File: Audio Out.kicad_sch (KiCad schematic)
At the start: 14 parts

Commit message: Fixed ultralibrarian library with capital letter difference
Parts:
- U9: footprint UltraLibrarian:D8_TEX -> Ultralibrarian:D8_TEX
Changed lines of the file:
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@@
       (effects (font (size 1.27 1.27)))
     )
-    (property "Footprint" "UltraLibrarian:D8_TEX" (at 131.445 52.705 0)
+    (property "Footprint" "Ultralibrarian:D8_TEX" (at 131.445 52.705 0)
       (effects (font (size 1.27 1.27)) hide)
     )
@@
       (effects (font (size 1.27 1.27)))
     )
-    (property "Footprint" "UltraLibrarian:D8_TEX" (at 131.445 106.045 0)
+    (property "Footprint" "Ultralibrarian:D8_TEX" (at 131.445 106.045 0)
       (effects (font (size 1.27 1.27)) hide)
     )
@@
       (effects (font (size 1.27 1.27)))
     )
-    (property "Footprint" "UltraLibrarian:D8_TEX" (at 156.21 144.78 0)
+    (property "Footprint" "Ultralibrarian:D8_TEX" (at 156.21 144.78 0)
       (effects (font (size 1.27 1.27)) hide)
     )

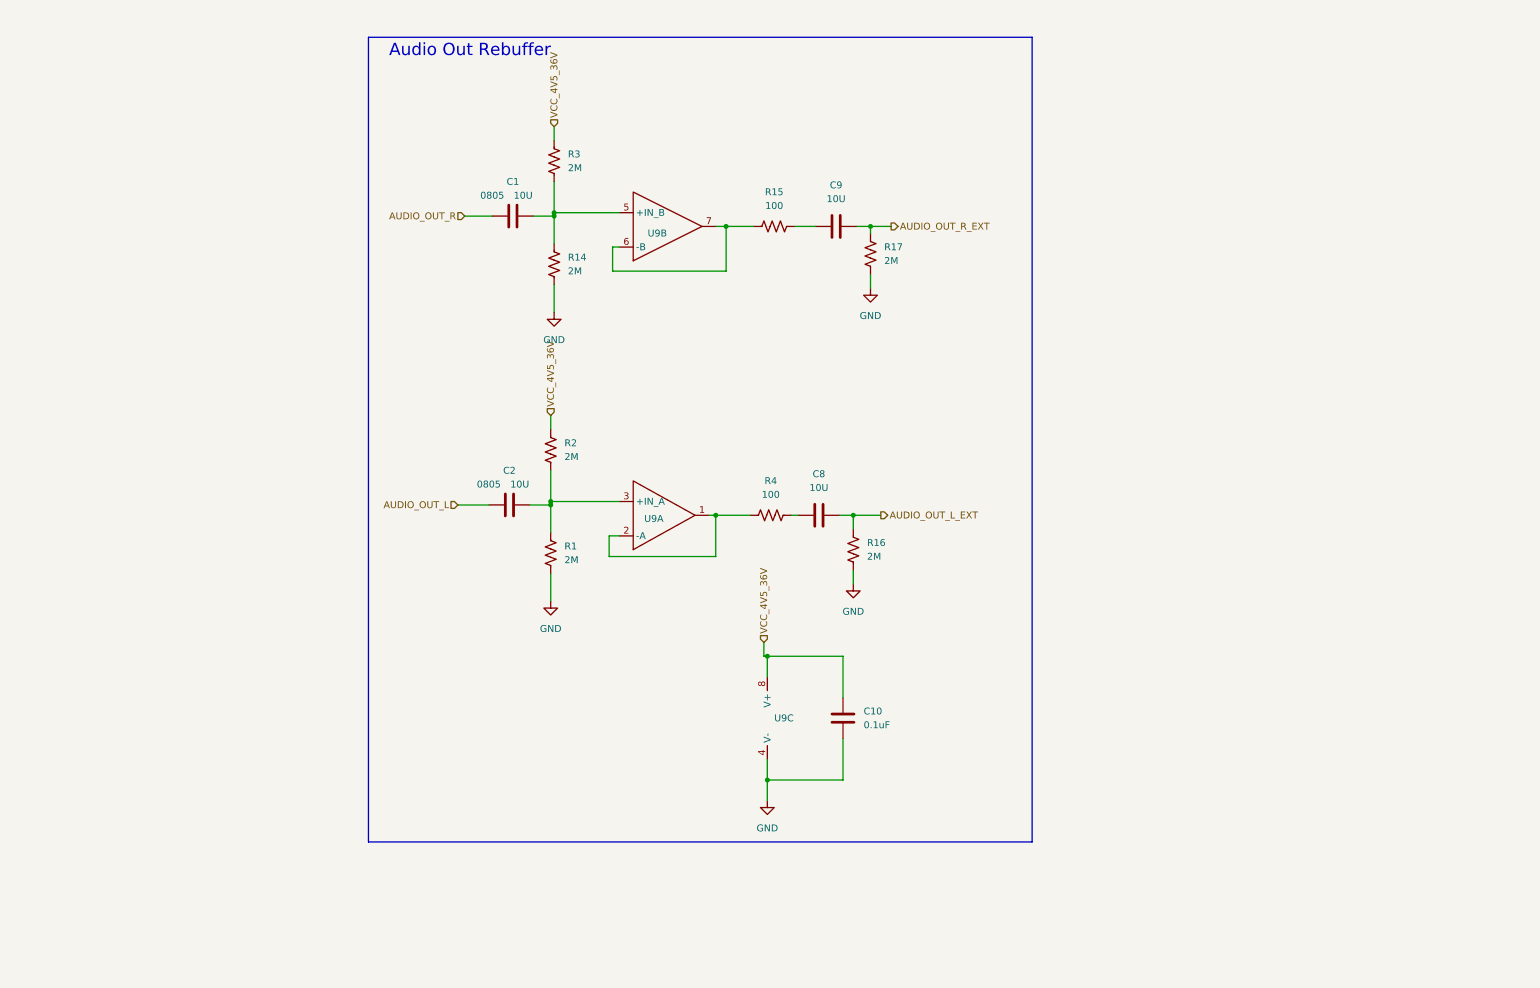
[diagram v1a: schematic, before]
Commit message: added knob headers, MIDI in header
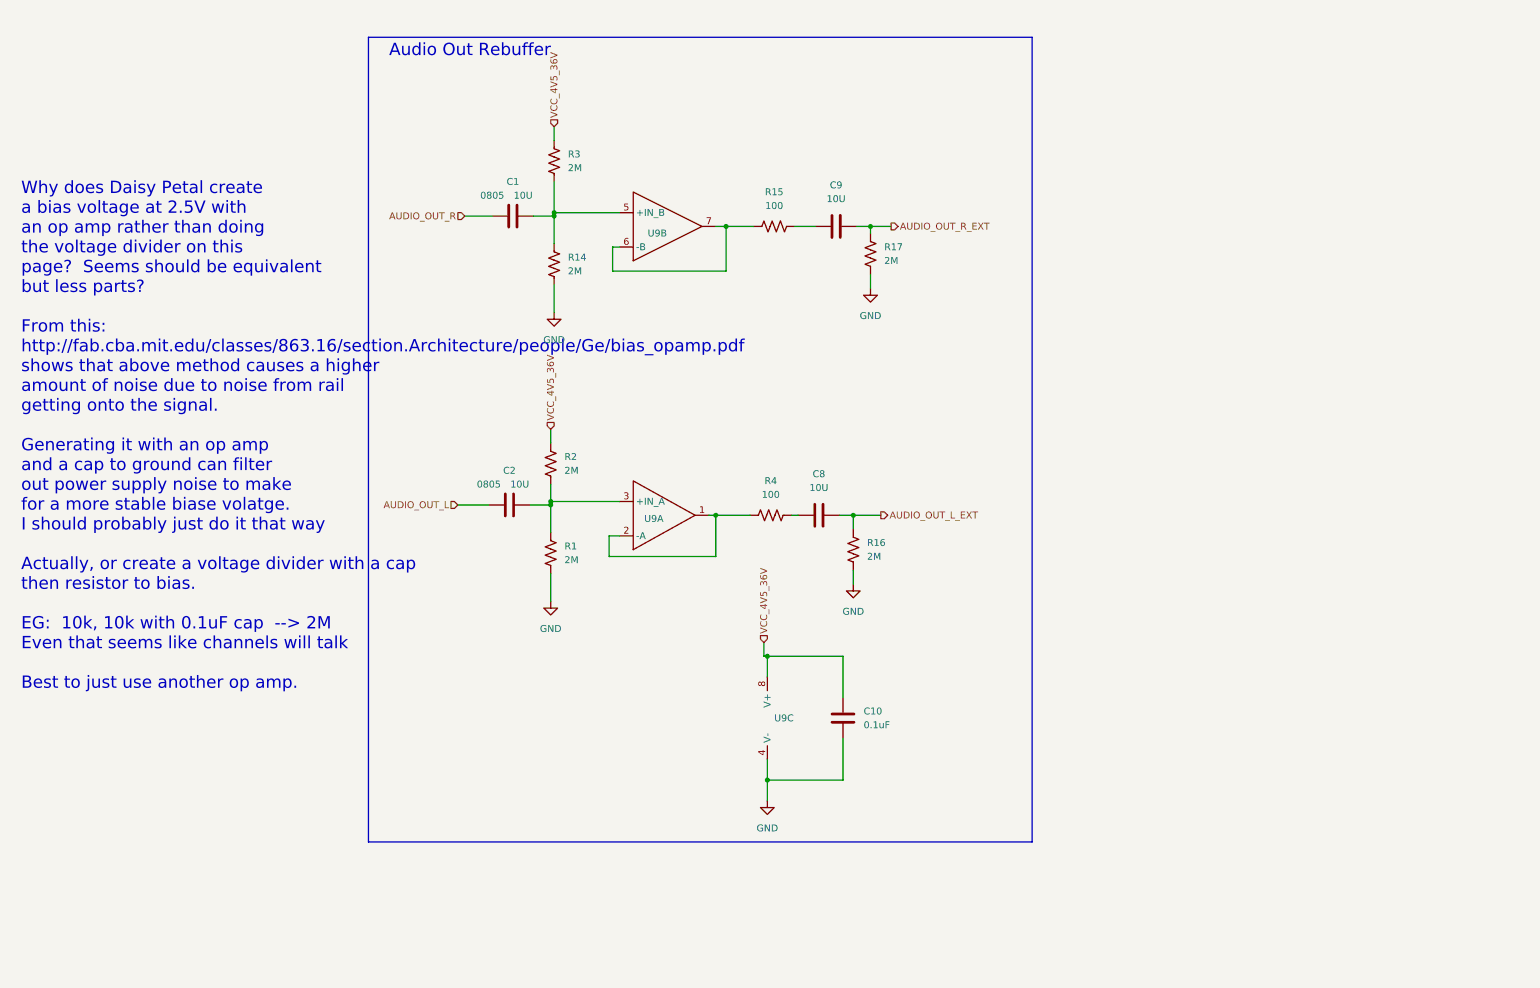
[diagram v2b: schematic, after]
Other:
- note added: "Why does Daisy Petal create a bias voltage at 2.5V with an op amp rather than doing the voltage divider on this page? Seems should be equivalent but less parts? From this: http://fab.cba.mit.edu/classes/863.16/section.Architecture/people/Ge/bias_opamp.pdf shows that above method causes a higher amount of noise due to noise from rail getting onto the signal. Generating it with an op amp and a cap 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"
- moved on the sheet: R2
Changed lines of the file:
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@@
     (stroke (width 0) (type default))
   )
-  (wire (pts (xy 113.665 97.79) (xy 113.665 103.505))
+  (wire (pts (xy 113.665 100.33) (xy 113.665 103.505))
     (stroke (width 0) (type default))
   )
@@
     (stroke (width 0) (type default))
   )
-  (wire (pts (xy 113.665 87.63) (xy 113.665 90.17))
+  (wire (pts (xy 113.665 90.17) (xy 113.665 92.71))
     (stroke (width 0) (type default))
   )
@@
     (effects (font (size 2.27 2.27)) (justify left bottom))
   )
+  (text "Why does Daisy Petal create\na bias voltage at 2.5V with\nan op amp rather than doing\nthe voltage divider on this\npage?  Seems should be equivalent\nbut less parts?\n\nFrom this:\nhttp://fab.cba.mit.edu/classes/863.16/section.Architecture/people/Ge/bias_opamp.pdf\nshows that above method causes a higher\namount of noise due to noise from rail\ngetting onto the signal.\n\nGenerating it with an op amp\nand a cap to ground can filter\nout power supply noise to make\nfor a more stable biase volatge.\nI should probably just do it that way\n\nActually, or create a voltage divider with a cap\nthen resistor to bias.\n\nEG:  10k, 10k with 0.1uF cap  --> 2M\nEven that seems like channels will talk\n\nBest to just use another op amp."
+    (at 15.875 138.43 0)
+    (effects (font (size 2.27 2.27)) (justify left bottom))
+  )
   (hierarchical_label "AUDIO_OUT_L" (shape input) (at 96.52 104.14 180) (fields_autoplaced)
     (effects (font (size 1.27 1.27)) (justify right))
   )
-  (hierarchical_label "VCC_4V5_36V" (shape input) (at 113.665 87.63 90) (fields_autoplaced)
+  (hierarchical_label "VCC_4V5_36V" (shape input) (at 113.665 90.17 90) (fields_autoplaced)
     (effects (font (size 1.27 1.27)) (justify left))
   )
@@
     )
   )
-  (symbol (lib_id "Device:R_US") (at 113.665 93.98 0) (unit 1)
-    (in_bom yes) (on_board yes) (dnp no) (fields_autoplaced)
-    (property "Reference" "R2" (at 116.205 92.71 0)
-      (effects (font (size 1.27 1.27)) (justify left))
-    )
-    (property "Value" "2M" (at 116.205 95.25 0)
-      (effects (font (size 1.27 1.27)) (justify left))
-    )
-    (property "Footprint" "Resistor_SMD:R_0402_1005Metric" (at 114.681 94.234 90)
-      (effects (font (size 1.27 1.27)) hide)
-    )
-    (property "Datasheet" "~" (at 113.665 93.98 0)
-      (effects (font (size 1.27 1.27)) hide)
-    )
+  (symbol (lib_id "Device:R_US") (at 113.665 96.52 0) (unit 1)
+    (in_bom yes) (on_board yes) (dnp no) (fields_autoplaced)
+    (property "Reference" "R2" (at 116.205 95.25 0)
+      (effects (font (size 1.27 1.27)) (justify left))
+    )
+    (property "Value" "2M" (at 116.205 97.79 0)
+      (effects (font (size 1.27 1.27)) (justify left))
+    )
+    (property "Footprint" "Resistor_SMD:R_0402_1005Metric" (at 114.681 96.774 90)
+      (effects (font (size 1.27 1.27)) hide)
+    )
+    (property "Datasheet" "~" (at 113.665 96.52 0)
+      (effects (font (size 1.27 1.27)) hide)
+    )

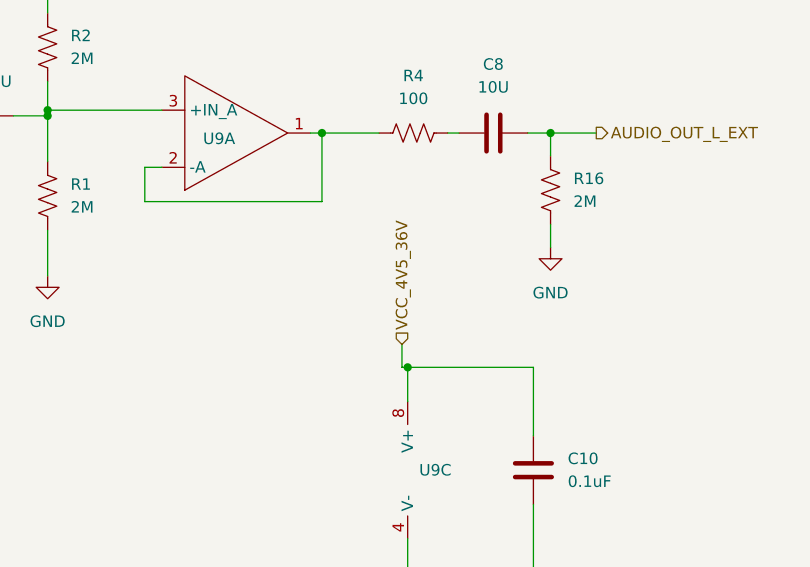
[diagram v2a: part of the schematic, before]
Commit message: Placeholder for speaker driver
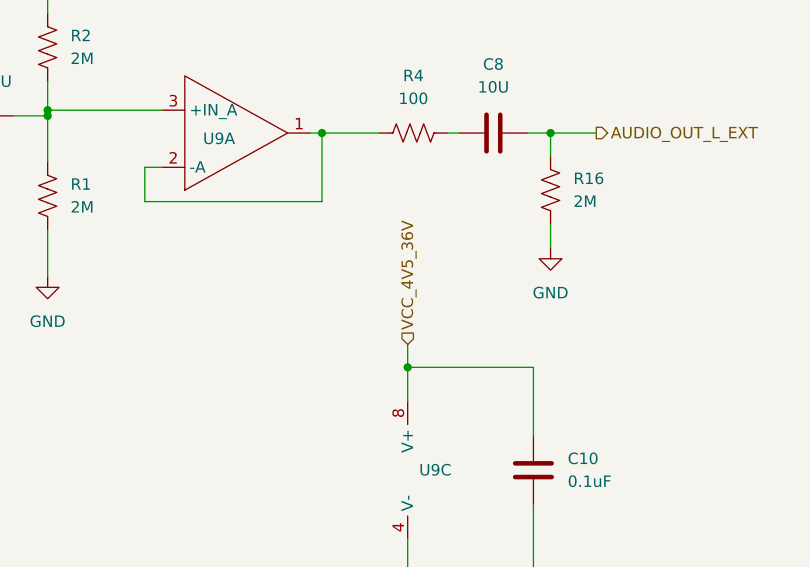
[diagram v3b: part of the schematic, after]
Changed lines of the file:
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@@
-    (stroke (width 0) (type default))
-  )
-  (wire (pts (xy 153.035 132.08) (xy 153.67 132.08))
     (stroke (width 0) (type default))
   )
@@
     (stroke (width 0) (type default))
   )
-  (wire (pts (xy 153.035 129.54) (xy 153.035 132.08))
+  (wire (pts (xy 153.67 129.54) (xy 153.67 132.08))
     (stroke (width 0) (type default))
   )
@@
     (effects (font (size 1.27 1.27)) (justify left))
   )
-  (hierarchical_label "VCC_4V5_36V" (shape input) (at 153.035 129.54 90) (fields_autoplaced)
+  (hierarchical_label "VCC_4V5_36V" (shape input) (at 153.67 129.54 90) (fields_autoplaced)
     (effects (font (size 1.27 1.27)) (justify left))
   )

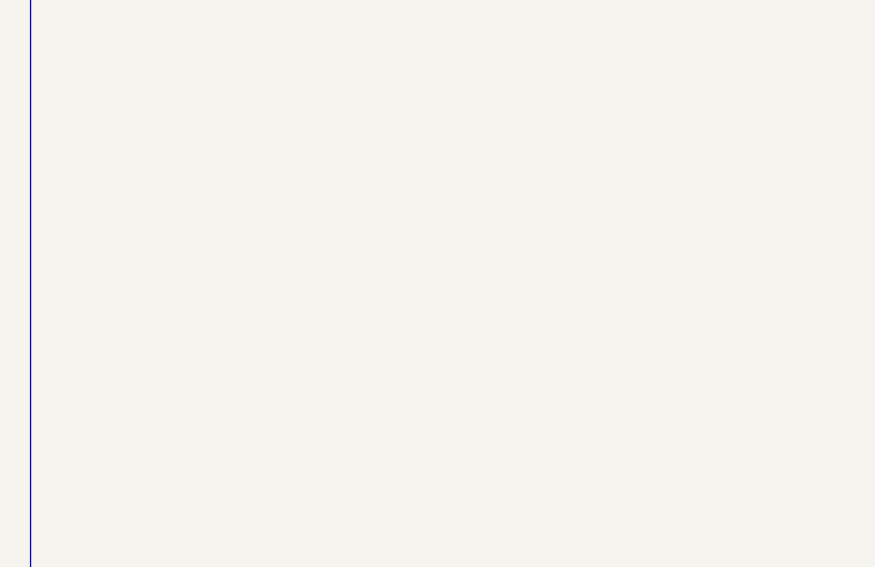
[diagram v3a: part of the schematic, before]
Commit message: Add USB 5V switcher, adjust audio in circuit
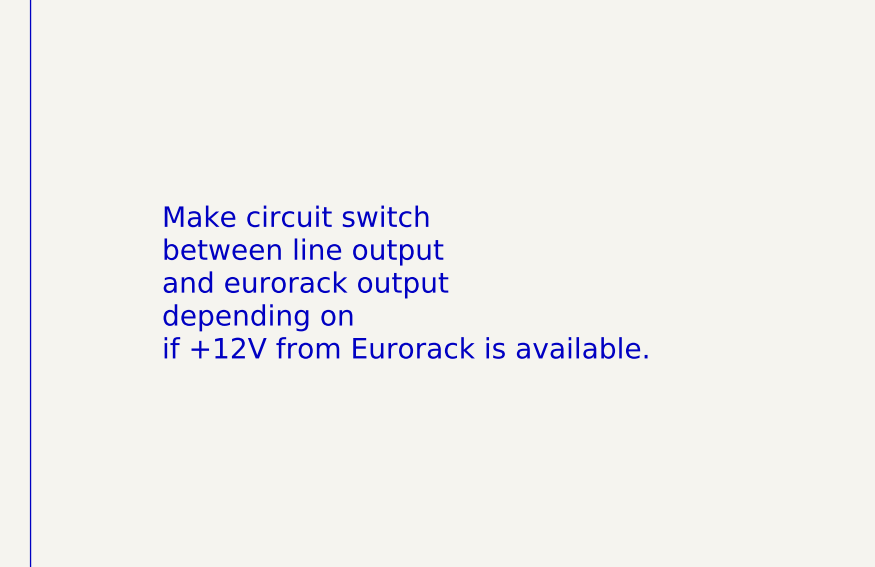
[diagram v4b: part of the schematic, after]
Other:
- note added: "Make circuit switch between line output and eurorack output depending on if +12V from Eurorack is available."
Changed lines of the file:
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@@
+    (effects (font (size 2.27 2.27)) (justify left bottom))
+  )
+  (text "Make circuit switch\nbetween line output\nand eurorack output\ndepending on\nif +12V from Eurorack is available."
+    (at 217.17 76.2 0)
     (effects (font (size 2.27 2.27)) (justify left bottom))
   )
